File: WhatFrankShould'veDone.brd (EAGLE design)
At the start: 90.5 x 66 mm, 52 parts, among them IC1 TLE5205-2G, IC2 TLE5205-2G, IC3 TLE5205-2G, IC5 TLE5205-2G, J3 POWERPOLE_DOUBLE, M0 Motor3, M1 Motor3, M2 Motor3, M3 Motor3, U1 LM2576.SMD

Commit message: blah
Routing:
- net PF4: track 39.8 -> 55.8 mm
- net PB0: track 107.9 -> 120.1 mm
- net PB1: track 112.4 -> 119.5 mm
- net +5V: track 83.8 -> 85.0 mm
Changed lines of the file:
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@@
 <wire x1="64.77" y1="39.37" x2="62.23" y2="39.37" width="0.4064" layer="16"/>
 <wire x1="62.23" y1="39.37" x2="59.69" y2="39.37" width="0.6096" layer="16"/>
-<wire x1="62.23" y1="39.37" x2="72.39" y2="39.37" width="0.6096" layer="16"/>
-<wire x1="72.39" y1="39.37" x2="73.025" y2="38.735" width="0.6096" layer="16"/>
-<wire x1="73.025" y1="38.735" x2="73.9775" y2="13.97" width="0.6096" layer="1"/>
+<wire x1="62.23" y1="39.37" x2="73.66" y2="39.37" width="0.6096" layer="16"/>
+<wire x1="73.66" y1="39.37" x2="74.295" y2="38.735" width="0.6096" layer="16"/>
+<wire x1="74.295" y1="38.735" x2="73.9775" y2="13.97" width="0.6096" layer="1"/>
 <wire x1="73.9775" y1="13.97" x2="73.025" y2="13.97" width="0.6096" layer="1"/>
 <wire x1="73.025" y1="13.97" x2="73.025" y2="7.62" width="0.4064" layer="1"/>
@@
 <contactref element="ENC1" pad="2"/>
 <wire x1="64.77" y1="34.29" x2="64.135" y2="34.29" width="0.254" layer="1"/>
-<wire x1="64.77" y1="34.29" x2="65.405" y2="34.29" width="0.254" layer="1"/>
-<wire x1="65.405" y1="34.29" x2="66.04" y2="33.655" width="0.254" layer="1"/>
-<wire x1="66.04" y1="33.655" x2="66.04" y2="13.335" width="0.254" layer="1"/>
-<wire x1="66.04" y1="13.335" x2="65.405" y2="12.7" width="0.254" layer="1"/>
-<wire x1="65.405" y1="12.7" x2="54.2925" y2="12.7" width="0.254" layer="1"/>
+<wire x1="64.77" y1="34.29" x2="64.77" y2="33.3375" width="0.254" layer="1"/>
+<wire x1="64.77" y1="33.3375" x2="71.755" y2="33.3375" width="0.254" layer="1"/>
+<wire x1="71.755" y1="33.3375" x2="71.755" y2="12.7" width="0.254" layer="1"/>
+<wire x1="71.755" y1="12.7" x2="54.2925" y2="12.7" width="0.254" layer="1"/>
 <wire x1="54.2925" y1="12.7" x2="53.6575" y2="12.065" width="0.254" layer="1"/>
 <wire x1="53.6575" y1="12.065" x2="53.6575" y2="9.8425" width="0.254" layer="1"/>
@@
 <contactref element="U$1" pad="PB1"/>
 <contactref element="ENC0" pad="2"/>
-<wire x1="67.31" y1="34.29" x2="68.58" y2="34.29" width="0.254" layer="1"/>
-<wire x1="68.58" y1="34.29" x2="69.215" y2="33.655" width="0.254" layer="1"/>
-<wire x1="69.215" y1="33.655" x2="69.215" y2="12.7" width="0.254" layer="1"/>
-<wire x1="69.215" y1="12.7" x2="68.58" y2="12.065" width="0.254" layer="1"/>
-<wire x1="68.58" y1="12.065" x2="55.5625" y2="12.065" width="0.254" layer="1"/>
+<wire x1="67.31" y1="34.29" x2="72.39" y2="34.29" width="0.254" layer="1"/>
+<wire x1="72.39" y1="34.29" x2="72.39" y2="12.065" width="0.254" layer="1"/>
+<wire x1="72.39" y1="12.065" x2="55.5625" y2="12.065" width="0.254" layer="1"/>
 <wire x1="55.5625" y1="12.065" x2="54.9275" y2="11.43" width="0.254" layer="1"/>
 <wire x1="54.9275" y1="11.43" x2="54.9275" y2="8.89" width="0.254" layer="1"/>
@@
 <contactref element="U$1" pad="PF4"/>
 <wire x1="45.72" y1="12.065" x2="45.72" y2="12.7" width="0.254" layer="1"/>
-<wire x1="62.23" y1="34.29" x2="62.865" y2="34.29" width="0.254" layer="1"/>
-<wire x1="62.865" y1="34.29" x2="63.5" y2="33.655" width="0.254" layer="1"/>
-<wire x1="63.5" y1="33.655" x2="63.5" y2="14.605" width="0.254" layer="1"/>
-<wire x1="63.5" y1="14.605" x2="62.865" y2="13.97" width="0.254" layer="1"/>
-<wire x1="62.865" y1="13.97" x2="46.99" y2="13.97" width="0.254" layer="1"/>
+<wire x1="62.23" y1="34.29" x2="62.23" y2="33.02" width="0.254" layer="1"/>
+<wire x1="62.23" y1="33.02" x2="63.5" y2="33.02" width="0.254" layer="1"/>
+<wire x1="63.5" y1="33.02" x2="63.5" y2="29.5275" width="0.254" layer="1"/>
+<wire x1="63.5" y1="29.5275" x2="71.12" y2="29.5275" width="0.254" layer="1"/>
+<wire x1="71.12" y1="29.5275" x2="71.12" y2="13.97" width="0.254" layer="1"/>
+<wire x1="71.12" y1="13.97" x2="46.99" y2="13.97" width="0.254" layer="1"/>
 <wire x1="46.99" y1="13.97" x2="45.72" y2="12.7" width="0.254" layer="1"/>
 </signal>

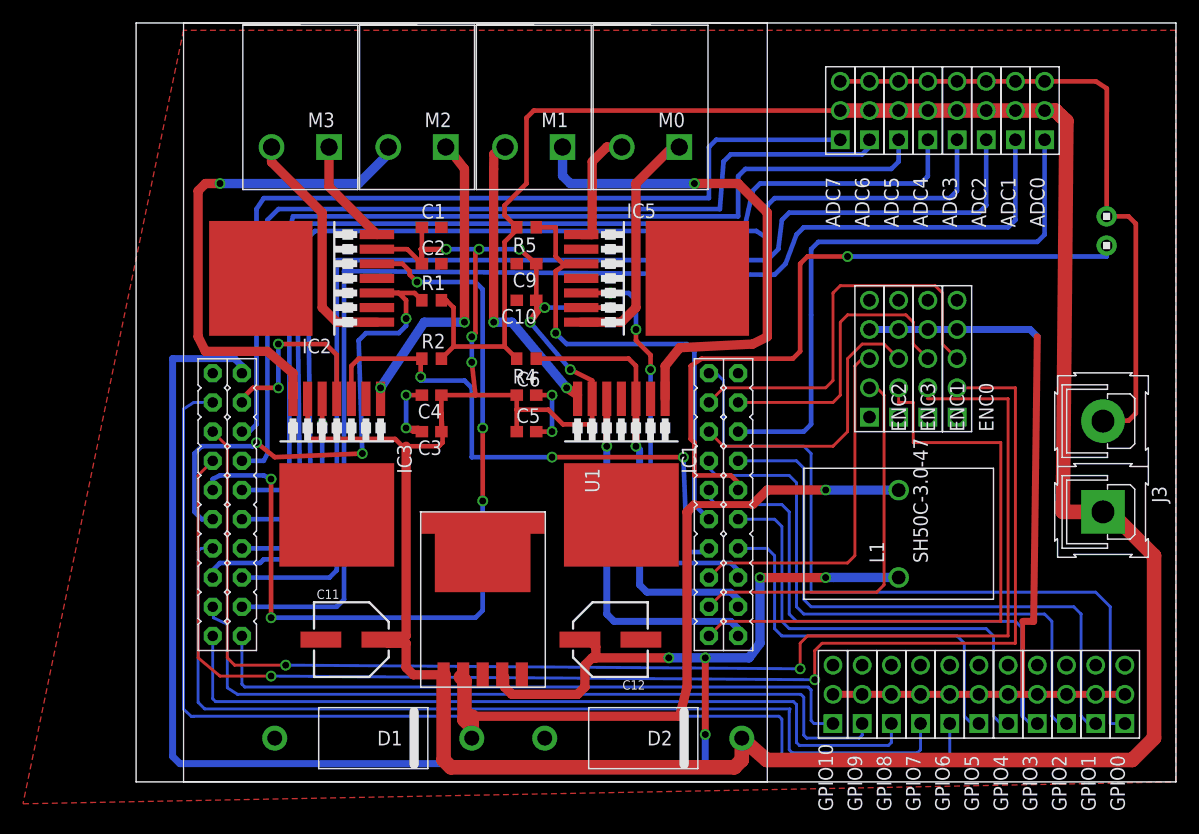
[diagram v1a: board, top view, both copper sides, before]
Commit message: Fixed angle errors
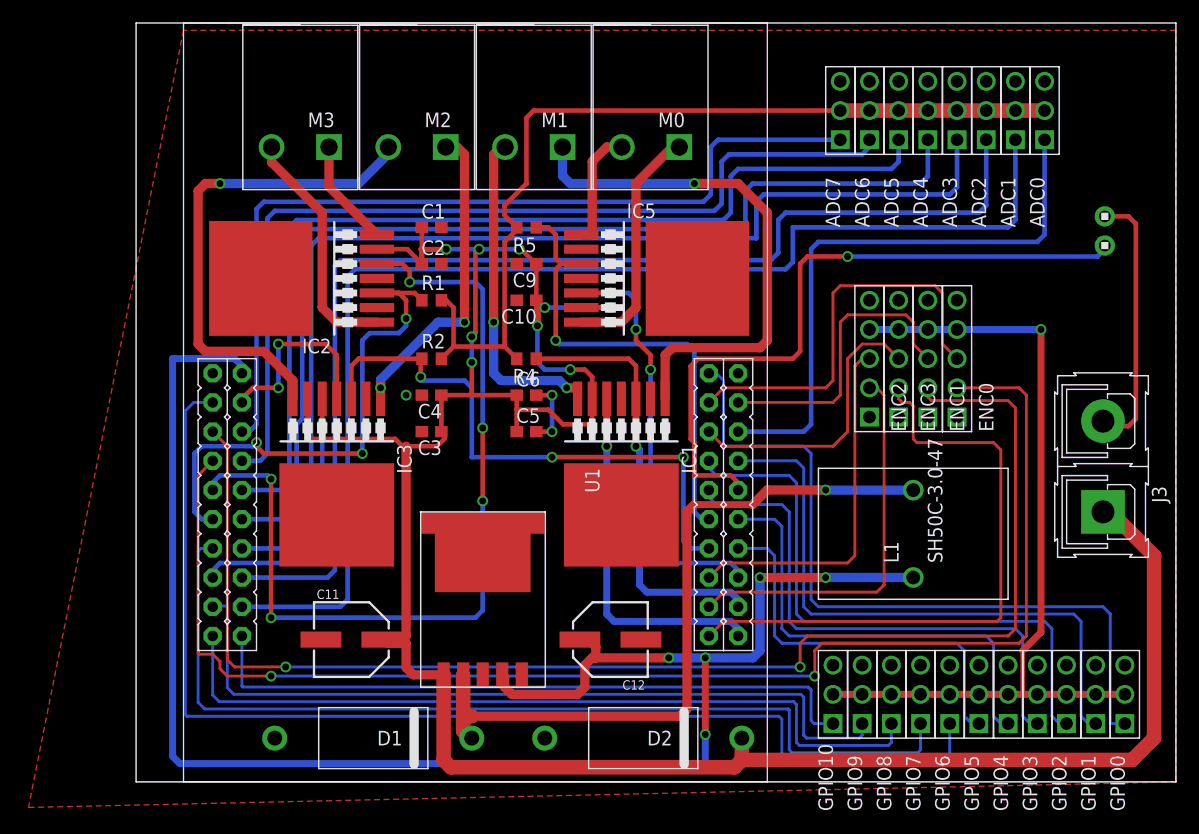
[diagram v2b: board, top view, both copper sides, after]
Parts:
- moved L1 1.27 mm to (63.5, 21.6)
- moved U$2 0.16 mm to (80.2, 46.7)
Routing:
- net V+: track 263.2 -> 221.1 mm
- net GND: track 87.0 -> 46.6 mm, vias 6 -> 5
- net N$8: track 26.0 -> 29.1 mm
- net VBUS: track 145.2 -> 146.8 mm
- net PE1: track 97.4 -> 96.3 mm
- net PF4: track 55.8 -> 54.7 mm
- net PB1: track 119.5 -> 120.5 mm
- net N$7: track 45.1 -> 46.0 mm
- net PD2: track 86.6 -> 85.8 mm
- net PA6: track 67.9 -> 68.5 mm
- net PE3: track 105.8 -> 106.5 mm
- net PC7: track 50.7 -> 50.1 mm
- net +5V: track 85.0 -> 85.4 mm, vias 0 -> 1

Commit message: Cleaned up airwires Added second ground plane Things missing:  Silkscreen comments  Mounting holes  Dounbhe check motor controller IC's pad connections
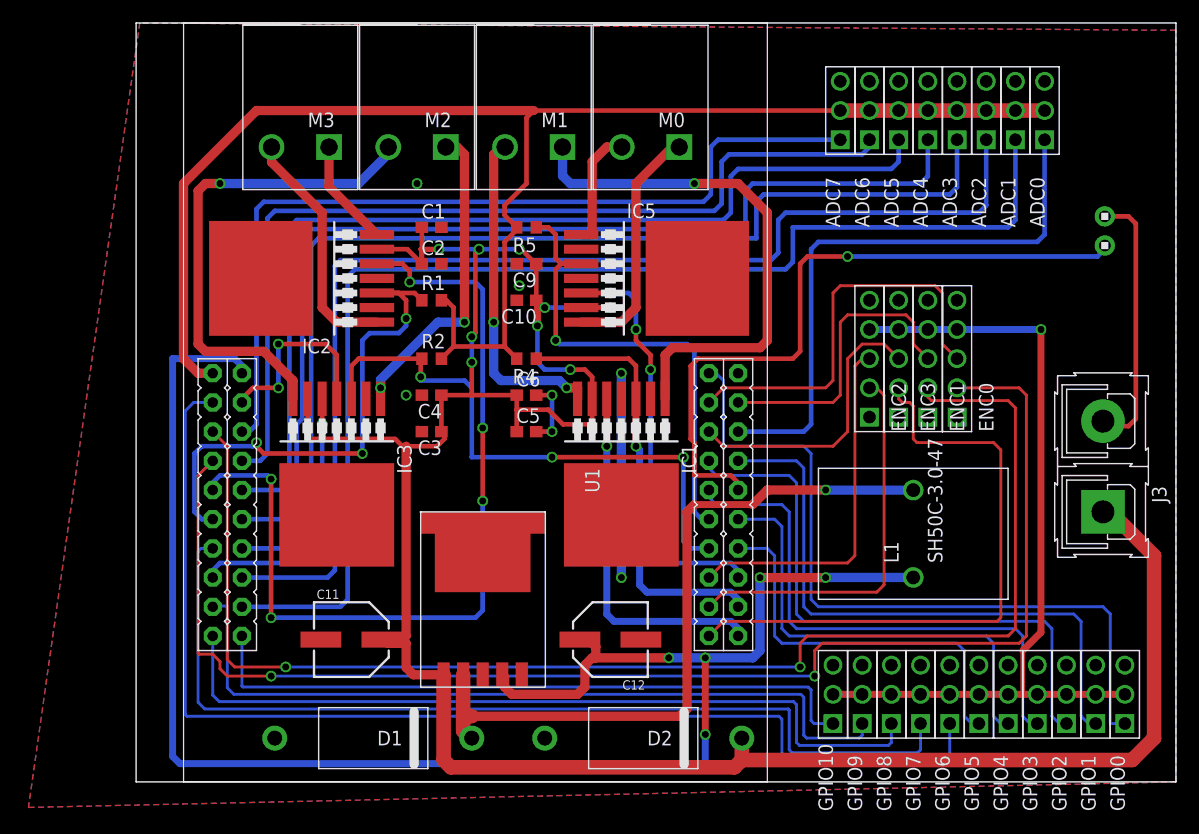
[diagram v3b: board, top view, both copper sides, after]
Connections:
- removed net 3.3V: U$1.3.3V
- net +3V3: now also U$1.3.3V
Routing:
- net +3V3: track 79.0 -> 130.5 mm
- net GND: track 46.6 -> 64.4 mm, vias 5 -> 9
- net V+: track 221.1 -> 220.4 mm
- added copper zone on layer 16, net GND
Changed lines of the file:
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@@
 <?xml version="1.0" encoding="utf-8"?>
 <!DOCTYPE eagle SYSTEM "eagle.dtd">
-<eagle version="6.3">
+<eagle version="6.4">
 <drawing>
 <settings>
@@
 <setting verticaltext="up"/>
 </settings>
-<grid distance="12.5" unitdist="mil" unit="mil" style="lines" multiple="1" display="no" altdistance="0.025" altunitdist="inch" altunit="mm"/>
+<grid distance="25" unitdist="mil" unit="mil" style="dots" multiple="2" display="yes" altdistance="5" altunitdist="mil" altunit="mil"/>
 <layers>
 <layer number="1" name="Top" color="4" fill="1" visible="yes" active="yes"/>
@@
 </elements>
 <signals>
-<signal name="3.3V">
-<contactref element="U$1" pad="3.3V"/>
-</signal>
-<signal name="GND" airwireshidden="yes">
+<signal name="GND">
 <contactref element="IC1" pad="4"/>
 <contactref element="C6" pad="2"/>
@@
 <vertex x="86.36" y="0"/>
 <vertex x="86.36" y="65.405"/>
-<vertex x="0" y="65.405"/>
+<vertex x="-3.81" y="66.04"/>
 </polygon>
 <contactref element="GPIO10" pad="3"/>
@@
 <contactref element="C12" pad="-"/>
 <contactref element="D1" pad="2"/>
-<wire x1="22.44" y1="48.26" x2="22.44" y2="45.085" width="0" layer="19" extent="1-1"/>
-<wire x1="62.23" y1="31.75" x2="64.77" y2="31.75" width="0" layer="19" extent="1-1"/>
-<wire x1="59.69" y1="31.75" x2="62.23" y2="31.75" width="0" layer="19" extent="1-1"/>
-<wire x1="28.995" y1="45.085" x2="34.6075" y2="43.815" width="0" layer="19" extent="1-1"/>
-<wire x1="29.4386" y1="9.3218" x2="31.4325" y2="3.81" width="0" layer="19" extent="1-1"/>
-<wire x1="38.1" y1="33.3375" x2="32.0675" y2="33.655" width="0" layer="19" extent="1-1"/>
+<via x="38.1" y="35.56" extent="1-16" drill="0.6" shape="octagon"/>
+<via x="38.1" y="17.78" extent="1-16" drill="0.6" shape="octagon"/>
+<wire x1="38.1" y1="17.78" x2="38.1" y2="35.56" width="0.8128" layer="16"/>
+<polygon width="0.4064" layer="16">
+<vertex x="-13.49375" y="-2.2225"/>
+<vertex x="86.36" y="0"/>
+<vertex x="86.36" y="65.405"/>
+<vertex x="-3.81" y="66.04"/>
+</polygon>
+<via x="29.21" y="43.18" extent="1-16" drill="0.6" shape="octagon"/>
+<via x="20.32" y="52.07" extent="1-16" drill="0.6" shape="octagon"/>
 </signal>
 <signal name="V+">
@@
 <wire x1="22.70125" y1="29.845" x2="22.70125" y2="30.48" width="0.4064" layer="1"/>
 <via x="29.21" y="46.355" extent="1-16" drill="0.6" shape="octagon"/>
-<wire x1="22.86" y1="46.355" x2="20.74" y2="46.355" width="0.4064" layer="1"/>
+<wire x1="22.225" y1="46.355" x2="20.74" y2="46.355" width="0.4064" layer="1"/>
 <wire x1="29.21" y1="46.355" x2="25.7175" y2="46.355" width="0.4064" layer="16"/>
 <via x="25.7175" y="46.355" extent="1-16" drill="0.6" shape="octagon"/>
 <wire x1="20.74" y1="45.085" x2="20.74" y2="46.2525" width="0.4064" layer="1"/>
 <wire x1="20.74" y1="46.2525" x2="20.6375" y2="46.355" width="0.4064" layer="1"/>
-<wire x1="20.6375" y1="46.355" x2="22.86" y2="46.355" width="0.4064" layer="1"/>
-<via x="22.86" y="46.355" extent="1-16" drill="0.6" shape="octagon"/>
-<wire x1="22.86" y1="46.355" x2="25.7175" y2="46.355" width="0.4064" layer="16"/>
+<wire x1="20.6375" y1="46.355" x2="22.225" y2="46.355" width="0.4064" layer="1"/>
+<via x="22.225" y="46.355" extent="1-16" drill="0.6" shape="octagon"/>
+<wire x1="22.225" y1="46.355" x2="25.7175" y2="46.355" width="0.4064" layer="16"/>
 <contactref element="C11" pad="+"/>
 <wire x1="22.6314" y1="9.3218" x2="22.86" y2="9.3218" width="0.8128" layer="1"/>
@@
 <wire x1="23.495" y1="41.275" x2="23.495" y2="37.885" width="0.4064" layer="1"/>
 <wire x1="59.69" y1="58.42" x2="62.23" y2="58.42" width="1.27" layer="1"/>
+<contactref element="U$1" pad="3.3V"/>
+<wire x1="2.54" y1="35.56" x2="1.27" y2="35.56" width="0.8128" layer="1"/>
+<wire x1="1.27" y1="35.56" x2="0" y2="36.83" width="0.8128" layer="1"/>
+<wire x1="0" y1="36.83" x2="0" y2="52.07" width="0.8128" layer="1"/>
+<wire x1="0" y1="52.07" x2="6.35" y2="58.42" width="0.8128" layer="1"/>
+<wire x1="6.35" y1="58.42" x2="30.48" y2="58.42" width="0.8128" layer="1"/>
 </signal>
 <signal name="N$7">

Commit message: Changed traces slightly
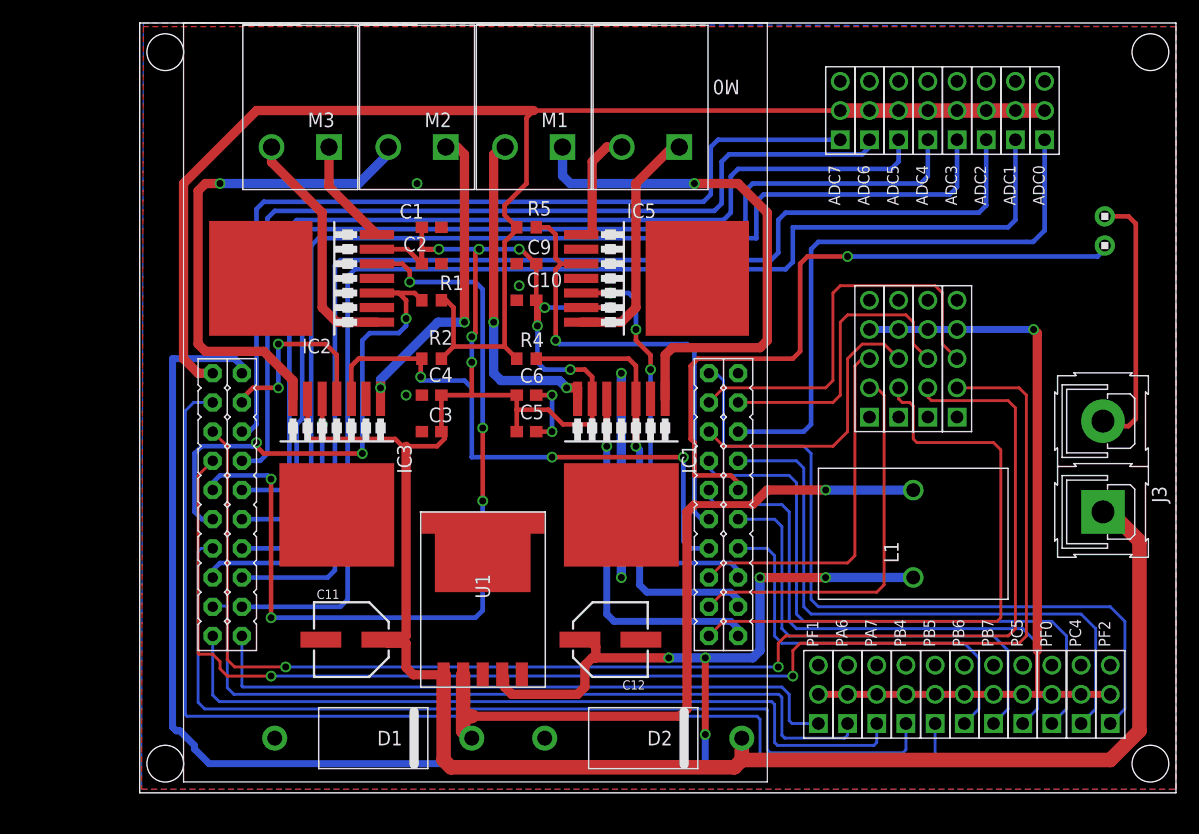
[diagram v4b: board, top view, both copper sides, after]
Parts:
- removed GPIO0, GPIO1, GPIO10, GPIO2, GPIO3, GPIO4, GPIO5, GPIO6, GPIO7, GPIO8, GPIO9: 3PINHEADER, RASEagleLib:3PINHEADER
- added PA6, PA7, PB4, PB5, PB6, PB7, PC4, PC5, PF0, PF1, PF2: 3PINHEADER, RASEagleLib:3PINHEADER
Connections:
- removed net GND: ADC0.3, ADC1.3, ADC2.3, ADC3.3, ADC4.3, ADC5.3, ADC6.3, ADC7.3, C1.2, C10.2, C11.-, C12.-, C2.2, C3.2, C4.2, C5.2, C6.2, C9.2, D1.2, D2.2, ENC0.1, ENC1.1, ENC2.1, ENC3.1, GPIO0.3, GPIO1.3, GPIO10.3, GPIO2.3, GPIO3.3, GPIO4.3, GPIO5.3, GPIO6.3, GPIO7.3, GPIO8.3, GPIO9.3, IC1.4, IC2.4, IC3.4, IC5.4, J3.2, U$1.GND1, U$1.GND2, U$2.2, U1.3, U1.5, U1.GROUND, U1.GROUND@1
- new net -GND: ADC0.3, ADC1.3, ADC2.3, ADC3.3, ADC4.3, ADC5.3, ADC6.3, ADC7.3, C1.2, C10.2, C11.-, C12.-, C2.2, C3.2, C4.2, C5.2, C6.2, C9.2, D1.2, D2.2, ENC0.1, ENC1.1, ENC2.1, ENC3.1, IC1.4, IC2.4, IC3.4, IC5.4, J3.2, PA6.3, PA7.3, PB4.3, PB5.3, PB6.3, PB7.3, PC4.3, PC5.3, PF0.3, PF1.3, PF2.3, U$1.GND1, U$1.GND2, U$2.2, U1.3, U1.5, U1.GROUND, U1.GROUND@1
- net +5V: now also PA6.2, PA7.2, PB4.2, PB5.2, PB6.2, PB7.2, PC4.2, PC5.2, PF0.2, PF1.2, PF2.2; no longer GPIO0.2, GPIO1.2, GPIO10.2, GPIO2.2, GPIO3.2, GPIO4.2, GPIO5.2, GPIO6.2, GPIO7.2, GPIO8.2, GPIO9.2
- net PA6: now also PA6.1; no longer GPIO9.1
- net PA7: now also PA7.1; no longer GPIO8.1
- net PB4: now also PB4.1; no longer GPIO7.1
- net PB5: now also PB5.1; no longer GPIO6.1
- net PB6: now also PB6.1; no longer GPIO5.1
- net PB7: now also PB7.1; no longer GPIO4.1
- net PC4: now also PF0.1; no longer GPIO2.1
- net PC5: now also PC5.1; no longer GPIO3.1
- net PF0: now also PC4.1; no longer GPIO1.1
- net PF1: now also PF1.1; no longer GPIO10.1
- net PF2: now also PF2.1; no longer GPIO0.1
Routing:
- net GND: track 64.4 -> 0.00 mm, vias 9 -> 0
- net -GND: track 0.00 -> 64.4 mm, vias 0 -> 9
- net V+: track 220.4 -> 217.0 mm
- net PF1: track 58.7 -> 57.2 mm
- net VBUS: track 146.8 -> 145.4 mm
- net PB5: track 102.2 -> 101.0 mm
- net PB4: track 83.6 -> 82.3 mm
- net PA7: track 69.7 -> 68.4 mm
- net PA6: track 68.5 -> 67.3 mm
- net +5V: track 85.4 -> 84.3 mm
- net PB6: track 34.7 -> 35.2 mm
- net PF0: track 52.5 -> 53.0 mm
- net PC4: track 52.1 -> 52.6 mm
- net PB7: track 39.8 -> 40.3 mm
- net PC5: track 47.0 -> 47.6 mm
- added copper zone on layer 1, net -GND
- added copper zone on layer 16, net -GND
- removed copper zone on layer 1, net GND
- removed copper zone on layer 16, net GND
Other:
- board size 90.5 x 66 mm -> 90.2 x 67 mm
- board text added: "-+3.3V"
- board text added: "-+5V"
- board text added: "-A"
- board text added: "-B"
- board text added: "-GND"
- board text added: "-Sig"
- board text added: "Reset-"
- board text added: "V+"
- board text added: "V-"
